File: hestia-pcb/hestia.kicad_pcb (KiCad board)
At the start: 4 copper layers, 90.2 x 95.9 mm, 184 parts, among them J1 Serial Connector, J12 B2B-ZR, J13 B2B-ZR, J14 B2B-ZR, J15 B2B-ZR, J16 B2B-ZR, J2 i2c connector, J3 ESQ-126-39-G-D, J4 ESQ-126-39-G-D, J5 VREF+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

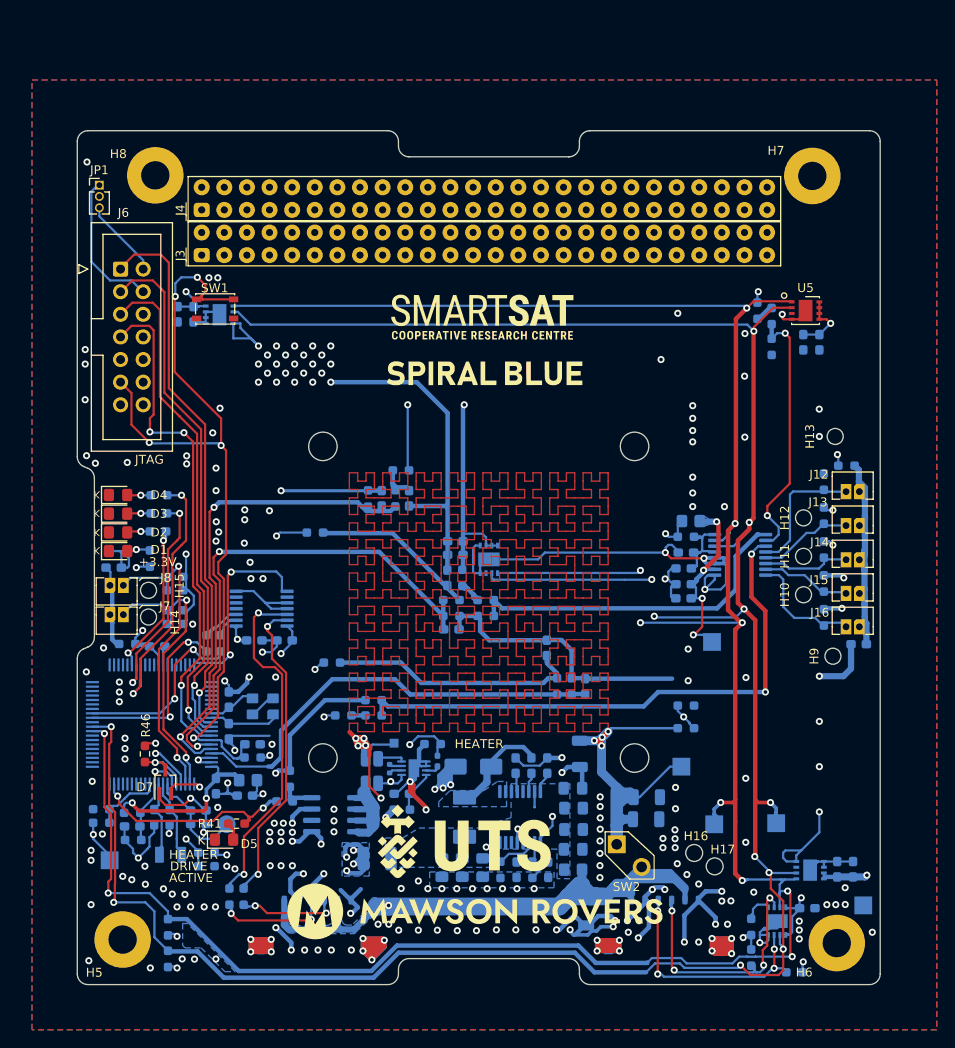
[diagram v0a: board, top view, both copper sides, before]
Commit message: #55: move holes H6, H7, H8 to align with PC/104
- move TP5, C54, U6, C29, C30 up to make room for H6 change
- simplify SCL_3.3V routing
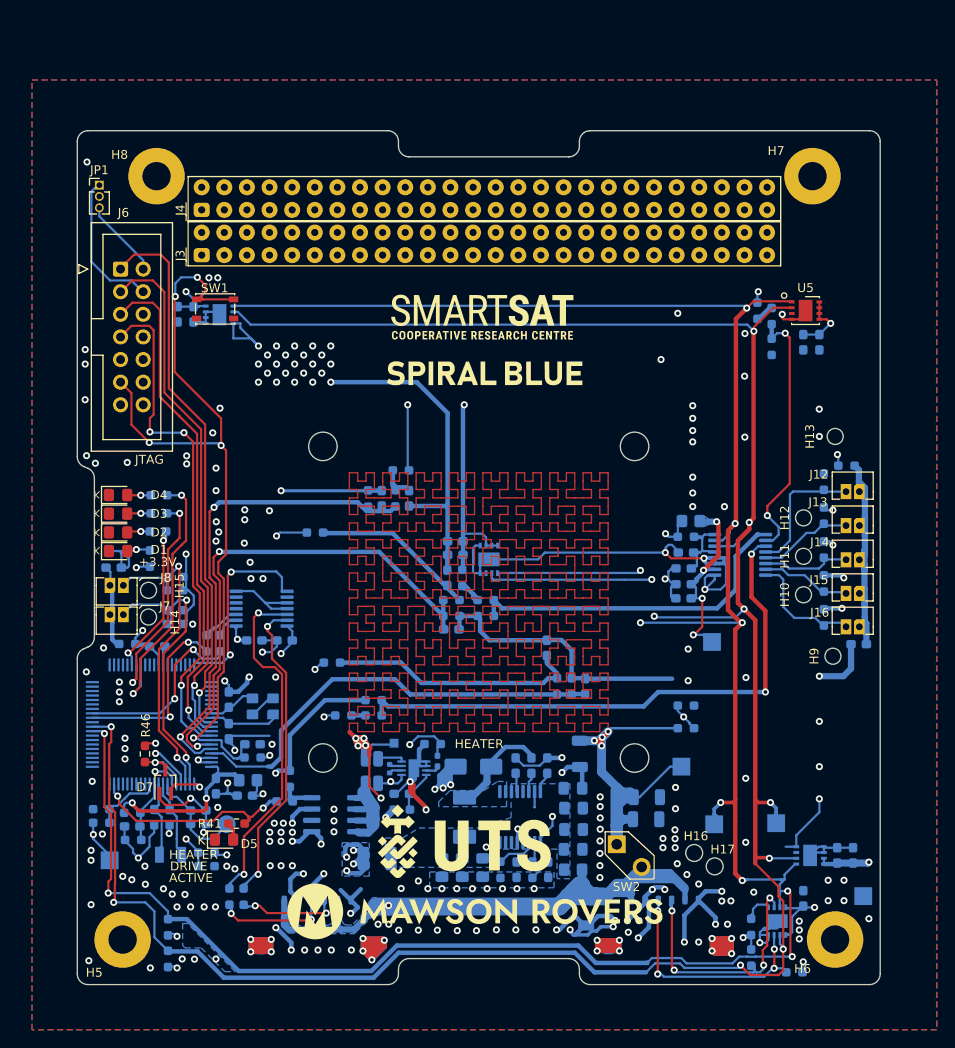
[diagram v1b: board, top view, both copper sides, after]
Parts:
- moved U6 1.65 mm to (183.9, 142.5)
- moved C29 1.55 mm to (186.9, 142.5)
- moved C30 1.55 mm to (188.7, 142.5)
- moved C54 1.19 mm to (183.1, 147.3), turned to 90 degrees
- moved TP5 1.04 mm to (189.9, 147.1)
- moved H6 0.44 mm to (186.7, 151.9)
- moved H8 0.17 mm to (110.5, 66.2)
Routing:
- net GND: track 393.5 -> 390.4 mm
- net /SCL_3.3V: track 295.9 -> 297.4 mm, vias 12 -> 11
- net /SDA_3.3V: track 295.8 -> 296.8 mm
- net +3.3V: track 127.5 -> 128.2 mm

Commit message: #55: move PC/104 connectors to align with template
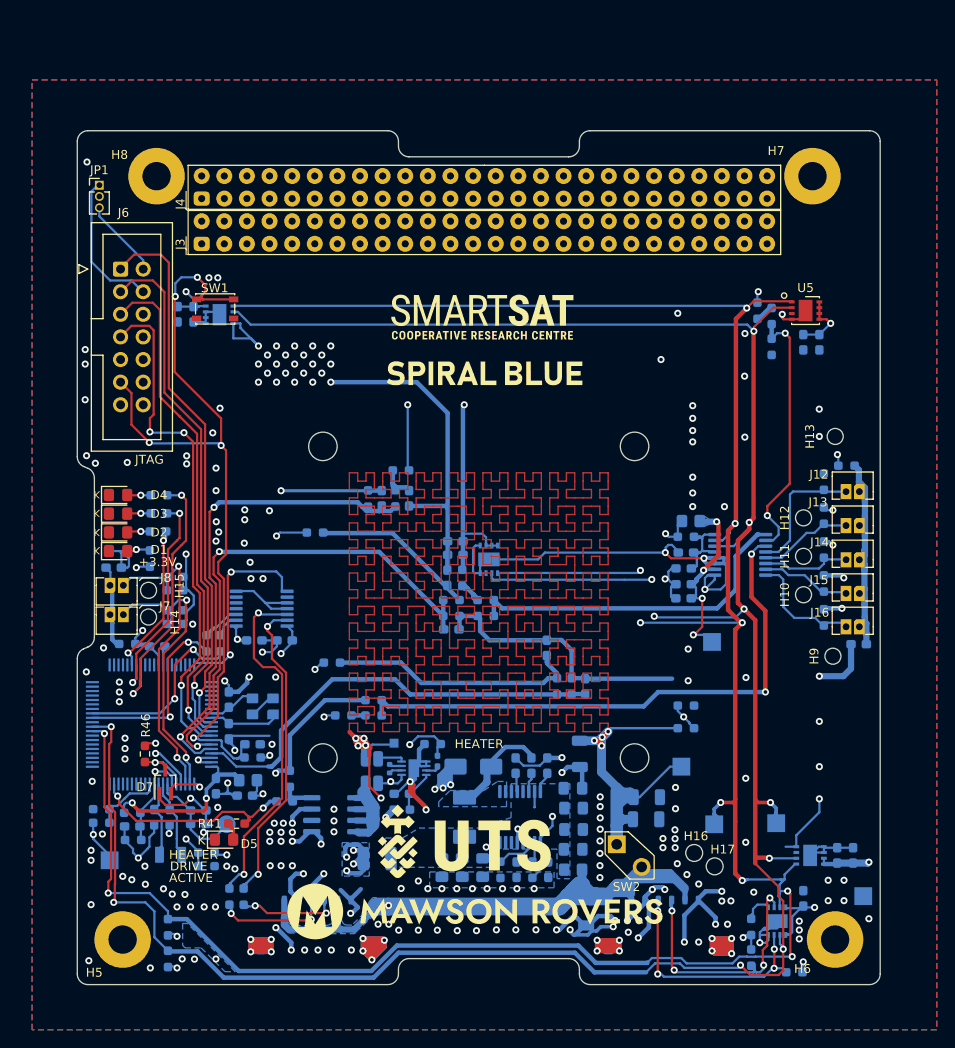
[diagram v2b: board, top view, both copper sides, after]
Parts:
- moved J3 1.27 mm to (147.3, 72.5)
- moved J4 1.27 mm to (147.3, 67.5)
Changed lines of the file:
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@@
   )
   (footprint "Hestia:ESQ-126-39-G-D" locked (layer "F.Cu")
-    (at 147.32 68.73)
+    (at 147.32 67.461466)
     (property "Sheetfile" "PC104.kicad_sch")
     (property "Sheetname" "PC104")
@@
     (property "exclude_from_bom" "")
     (attr through_hole exclude_from_bom)
-    (fp_text reference "J4" (at -34.1386 1.2931 90 unlocked) (layer "F.SilkS")
+    (fp_text reference "J4" (at -34.1386 1.880534 90 unlocked) (layer "F.SilkS")
         (effects (font (size 1 1) (thickness 0.15)))
     )
@@
   )
   (footprint "Hestia:ESQ-126-39-G-D" locked (layer "F.Cu")
-    (at 147.32 73.81)
+    (at 147.32 72.541466)
     (property "Sheetfile" "PC104.kicad_sch")
     (property "Sheetname" "PC104")
@@
   (segment (start 176.0814 154.8231) (end 177.1814 155.9231) (width 0.25) (layer "F.Cu") (net 183))
   (segment (start 178.054 136.553) (end 177.7365 136.2355) (width 0.4) (layer "F.Cu") (net 183))
-  (segment (start 179.436 142.819) (end 179.324 142.819) (width 0.5) (layer "F.Cu") (net 183))
   (segment (start 105.8164 145.7351) (end 105.8164 147.6401) (width 0.25) (layer "F.Cu") (net 183))
   (segment (start 105.8418 145.7097) (end 105.8164 145.7351) (width 0.25) (layer "F.Cu") (net 183))
@@
   (segment (start 105.8418 137.631782) (end 105.8418 145.7097) (width 0.25) (layer "F.Cu") (net 183))
   (segment (start 177.0634 105.0951) (end 177.546 104.6125) (width 0.5) (layer "F.Cu") (net 183))
-  (segment (start 179.253 142.748) (end 179.324 142.819) (width 0.4) (layer "F.Cu") (net 183))
   (segment (start 180.34 145.99685) (end 177.7365 143.39335) (width 0.25) (layer "F.Cu") (net 183))
   (segment (start 177.546 83.6585) (end 177.5814 83.6231) (width 0.5) (layer "F.Cu") (net 183))
   (segment (start 179.7715 80.983) (end 181.838 80.983) (width 0.25) (layer "F.Cu") (net 183))
   (segment (start 177.7365 116.0782) (end 177.7365 136.2355) (width 0.5) (layer "F.Cu") (net 183))
+  (segment (start 177.7365 142.748) (end 179.253 142.748) (width 0.5) (layer "F.Cu") (net 183))
   (segment (start 177.0634 105.0951) (end 177.0634 105.8571) (width 0.5) (layer "F.Cu") (net 183))
   (segment (start 105.1814 129.9871) (end 105.1814 136.971382) (width 0.25) (layer "F.Cu") (net 183))
   (segment (start 180.8814 147.6231) (end 180.34 147.0817) (width 0.25) (layer "F.Cu") (net 183))
-  (segment (start 177.7365 142.748) (end 179.253 142.748) (width 0.4) (layer "F.Cu") (net 183))
   (segment (start 177.5814 83.1731) (end 179.7715 80.983) (width 0.25) (layer "F.Cu") (net 183))
   (via (at 176.4814 114.8231) (size 0.8) (drill 0.4) (layers "F.Cu" "B.Cu") (net 183))

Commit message: #55: move drill origin to (100,150)
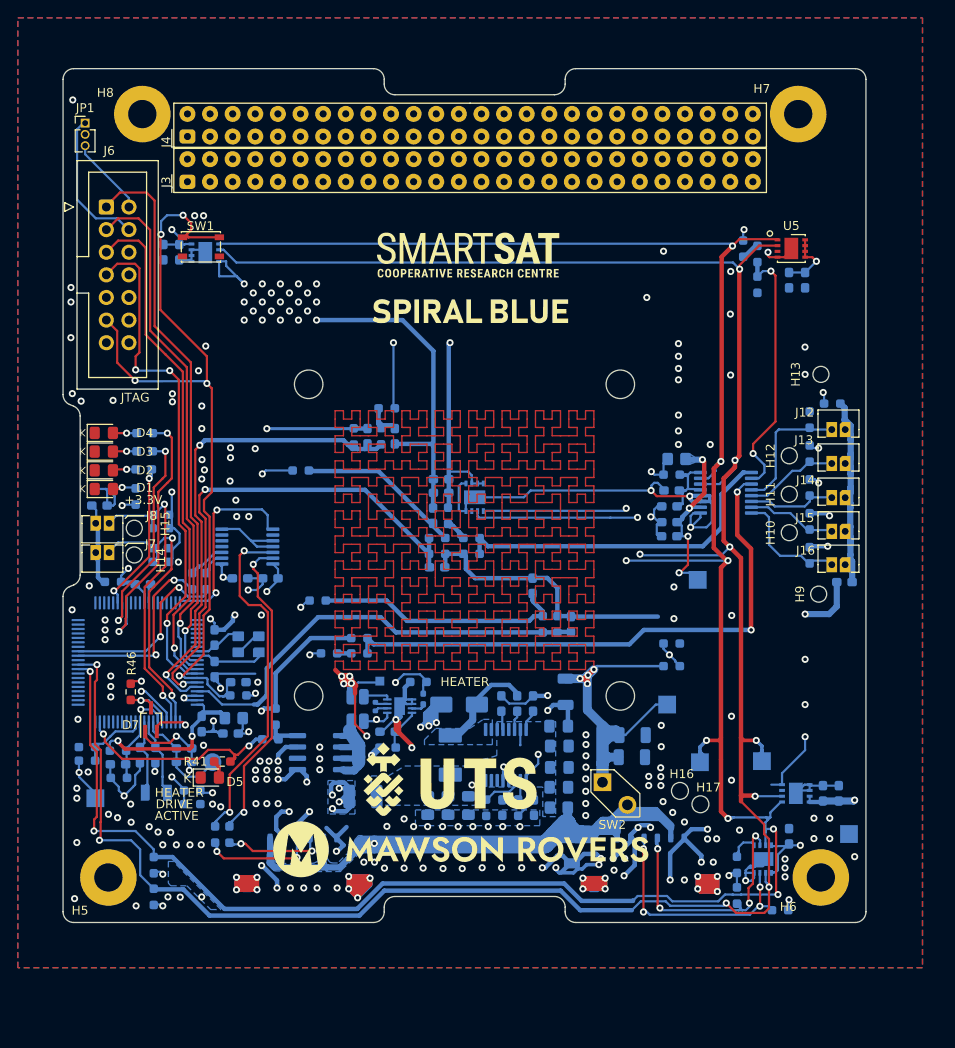
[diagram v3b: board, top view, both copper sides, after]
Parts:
- moved C26 7.15 mm to (155.7, 132.6)
- moved C33 7.15 mm to (155.7, 130.2)
- moved C38 7.15 mm to (152.9, 137.1)
- moved C42 7.15 mm to (142.0, 110.1)
- moved C7 7.15 mm to (156.4, 124.1)
- moved FB13 7.15 mm to (136.5, 130.4)
- moved LOGO2 7.15 mm to (143.5, 133.9)
- moved LOGO4 7.15 mm to (145.7, 81.4)
- moved Q1 7.15 mm to (128.8, 131.0)
- moved R13 7.15 mm to (155.5, 116.5)
- moved R26 7.15 mm to (130.9, 122.0)
- moved R27 7.15 mm to (140.5, 124.9)
- moved TP4 7.15 mm to (178.5, 131.9)
- moved TP5 7.15 mm to (188.3, 140.1)
- moved C12 7.15 mm to (108.6, 131.2)
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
